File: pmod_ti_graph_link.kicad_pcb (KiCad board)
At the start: 2 copper layers, 25.9 x 20.3 mm, 11 parts, among them J1 Pmod Peripheral, J2 Graph Link, J3 Link Debug, Q1 UMH4N

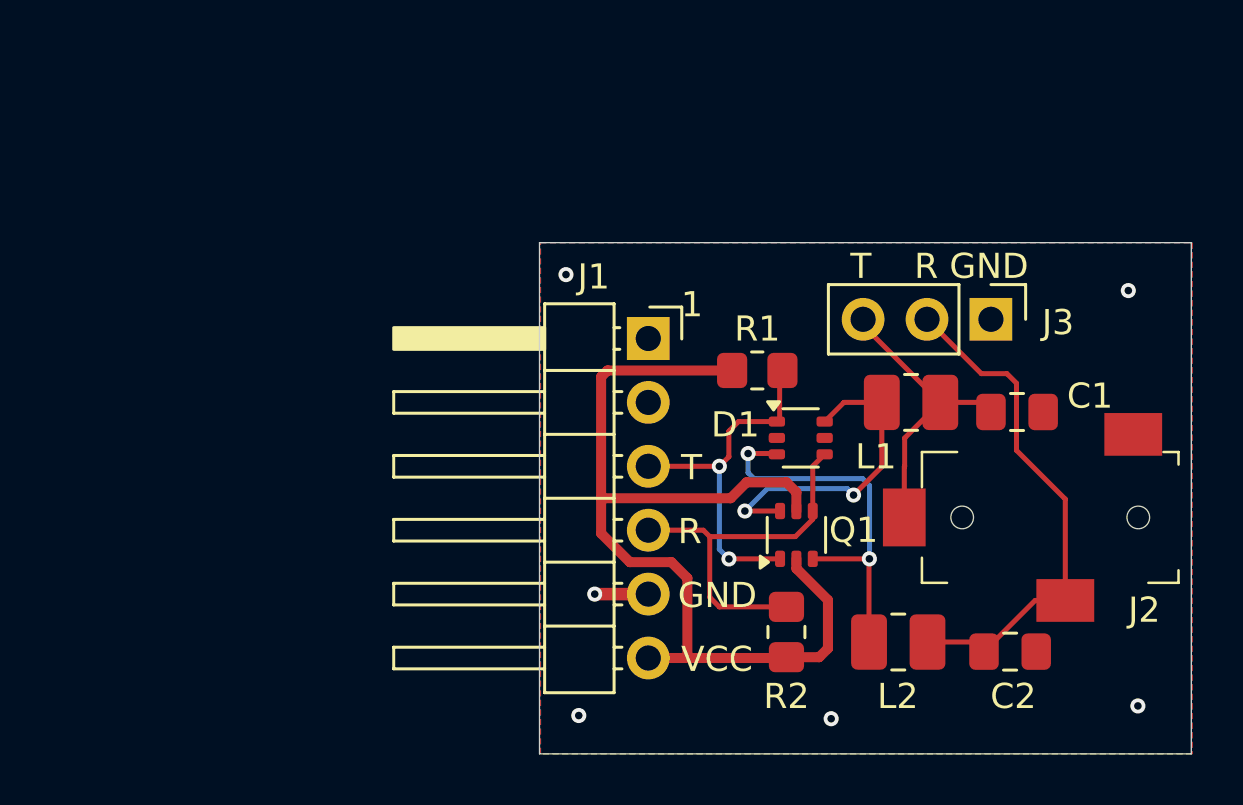
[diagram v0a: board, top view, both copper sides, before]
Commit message: Clean up routing, add GND vias, add text
- Clean up routing around transistor and diode
- Add stitching GND vias around perimeter
- Add "Pmod TI Graph Link" text and date
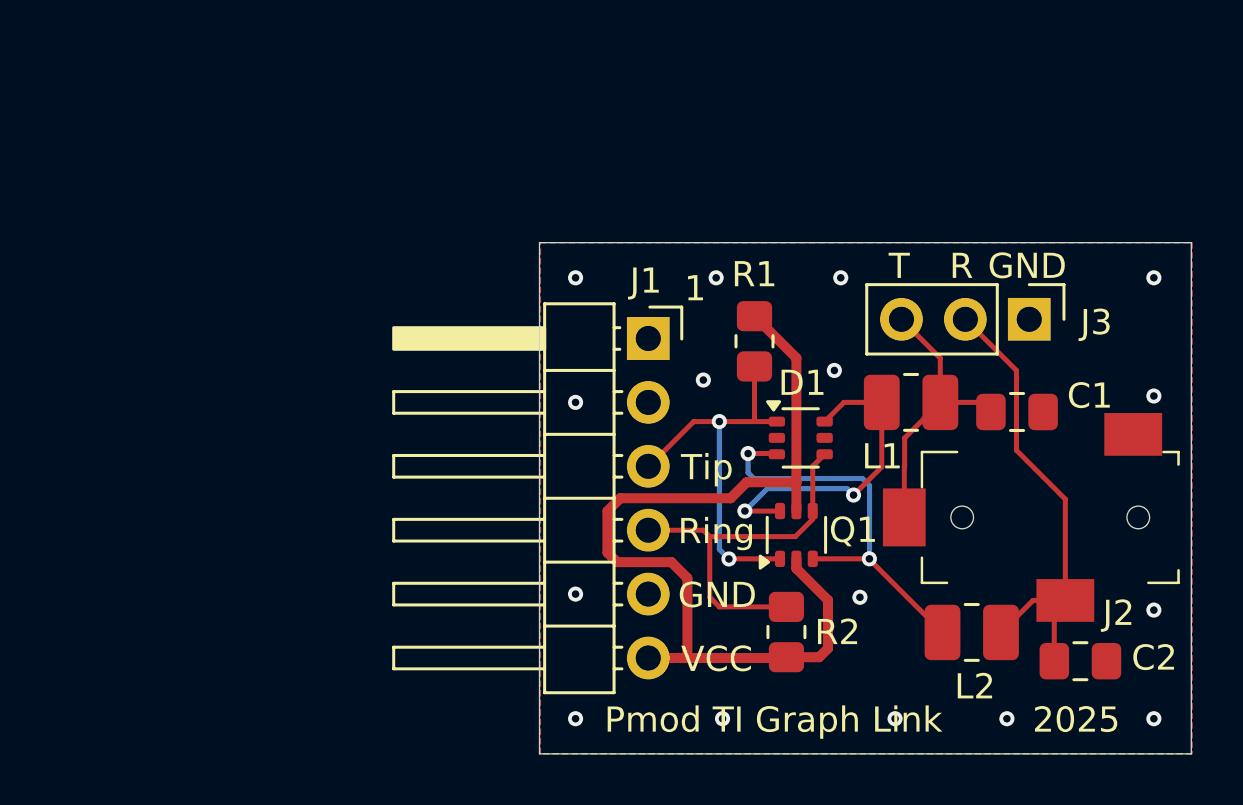
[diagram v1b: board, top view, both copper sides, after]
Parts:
- moved L2 2.95 mm to (157.6, 104.4)
- moved C2 2.82 mm to (161.9, 105.5)
- moved J3 1.52 mm to (159.9, 91.9)
- moved R1 1.16 mm to (149.0, 92.8), turned to -90 degrees
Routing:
- net VCC: track 39.2 -> 36.2 mm
- net GND: track 2.16 -> 0.00 mm, vias 6 -> 16
- net /DBus_Ring: track 20.5 -> 18.5 mm
- net /Pmod_Tip: track 14.5 -> 15.7 mm
- net Net-(D1B-K): track 15.5 -> 16.3 mm
- net /DBus_Tip: track 11.9 -> 11.3 mm
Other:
- board text added: "2025"
- board text added: "Pmod TI Graph Link"
- board text added: "Ring"
- board text added: "Tip"

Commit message: Add inductor shield->GND and clean up placement and routing. Prelim "Rev A"
- Add optional inductor between 2.5mm shield and GND
- Make VCC thicker, update calc icon, clean up traces
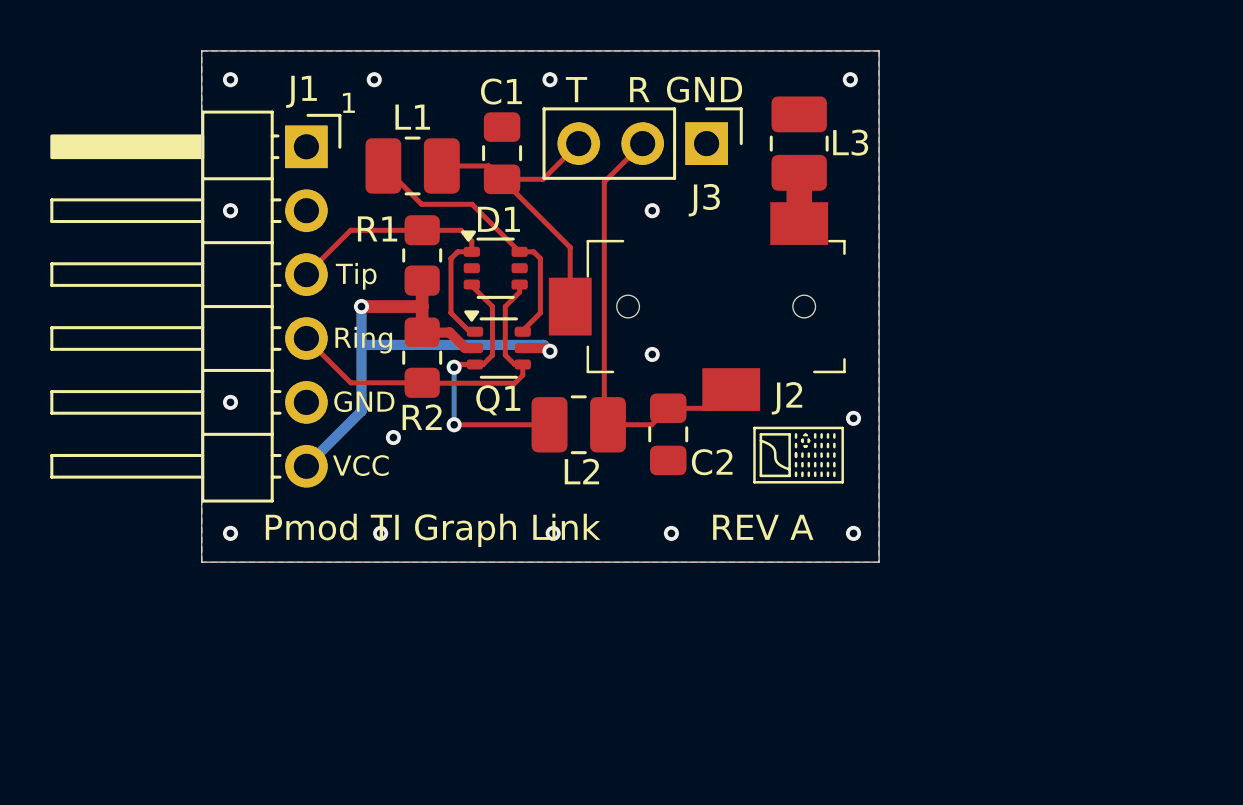
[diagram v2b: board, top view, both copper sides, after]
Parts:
- added L3: 2.7, Inductor_SMD:L_1008_2520Metric_Pad1.43x2.20mm_HandSolder, F.Cu at (150.7, 85.0)
- Q1: value UMH4N -> RN1911
- moved C1 22.9 mm to (138.9, 85.3), turned to 90 degrees
- moved L1 21.9 mm to (135.4, 85.9)
- moved C2 18.7 mm to (145.5, 96.5), turned to -90 degrees
- moved R2 18.1 mm to (135.8, 93.5), turned to -90 degrees
- moved L2 17.7 mm to (142.0, 96.1)
- moved J2 15.7 mm to (147.4, 91.4)
- moved J1 15.6 mm to (131.2, 85.0)
- moved J3 14.6 mm to (147.1, 85.0)
- moved Q1 14.0 mm to (138.8, 93.1), turned to 0 degrees
- moved D1 13.9 mm to (138.7, 89.9)
- moved R1 13.6 mm to (135.8, 89.4), turned to 90 degrees
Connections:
- J2 pad S: GND -> Net-(J2-PadS)
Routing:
- net VCC: track 36.2 -> 22.6 mm, vias 0 -> 2
- net Net-(D1B-K): track 16.3 -> 10.9 mm
- net /Pmod_Tip: track 15.7 -> 12.3 mm, vias 2 -> 0
- net Net-(J2-PadS): track 0.00 -> 2.02 mm
- net Net-(D1A-K): track 12.9 -> 11.0 mm, vias 2 -> 0
- net /Pmod_Ring: track 15.3 -> 13.8 mm
- net /DBus_Tip: track 11.3 -> 12.4 mm
- net /DBus_Ring: track 18.5 -> 17.6 mm
- net GND: vias 16 -> 15
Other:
- board size 25.9 x 20.3 mm -> 26.9 x 20.3 mm
- board text added: "REV A"
- board text removed: "2025"
